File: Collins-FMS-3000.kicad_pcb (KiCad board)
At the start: 2 copper layers, 145 x 161 mm, 142 parts, among them J1 USB_B_Mini, J2 AVR-ISP-6, J3 Conn_02x04_Odd_Even, SW1 SW_Push_LED, SW10 SW_Push_LED, SW11 SW_Push_LED, SW12 SW_Push_LED, SW13 SW_Push_LED, SW14 SW_Push_LED, SW15 SW_Push_LED, SW16 SW_Push_LED, SW17 SW_Push_LED, SW18 SW_Push_LED, SW19 SW_Push_LED, SW2 SW_Push_LED, SW20 SW_Push_LED, SW21 SW_Push_LED, SW22 SW_Push_LED, SW23 SW_Push_LED, SW24 SW_Push_LED, SW25 SW_Push_LED, SW26 SW_Push_LED, SW27 SW_Push_LED, SW28 SW_Push_LED, SW29 SW_Push_LED, SW3 SW_Push_LED, SW30 SW_Push_LED, SW31 SW_Push_LED, SW32 SW_Push_LED, SW33 SW_Push_LED, SW34 SW_Push_LED, SW35 SW_Push_LED, SW36 SW_Push_LED, SW37 SW_Push_LED, SW38 SW_Push_LED, SW39 SW_Push_LED, SW4 SW_Push_LED, SW40 SW_Push_LED, SW41 SW_Push_LED, SW42 SW_Push_LED, SW43 SW_Push_LED, SW44 SW_Push_LED, SW45 SW_Push_LED, SW46 SW_Push_LED, SW47 SW_Push_LED, SW48 SW_Push_LED, SW49 SW_Push_LED, SW5 SW_Push_LED, SW50 SW_Push_LED, SW51 SW_Push_LED, SW52 SW_Push_LED, SW53 SW_Push_LED, SW54 SW_Push_LED, SW55 SW_Push_LED, SW56 SW_Push_LED, SW57 SW_Push_LED, SW58 SW_Push_LED, SW59 SW_Push_LED, SW6 SW_Push_LED, SW60 SW_Push_LED, SW61 SW_Push_LED, SW62 SW_Push_LED, SW63 SW_Push_LED, SW64 SW_Push_LED, SW65 SW_Push_LED, SW66 SW_Push_LED, SW67 SW_Push_LED, SW68 SW_Push_LED, SW69 SW_Push_LED, SW7 SW_Push_LED, SW8 SW_Push_LED, SW9 SW_Push_LED, U1 ATmega32U4-MU, U2 MCP23017_SO, U3 MCP23017_SO, U4 IS31FL3733B, Y1 16MHz

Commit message: More routing
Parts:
- R10, R11, R12, R13, R14, R15, R16, R17, R18, R19, R8, R9: moved to B.Cu
- moved R10 19.3 mm to (170.0, 61.2)
- moved R13 19.3 mm to (173.2, 61.2)
- moved R16 19.3 mm to (176.3, 61.2)
- moved R8 18.8 mm to (167.1, 60.7)
- moved R12 15.2 mm to (170.0, 59.2)
- moved R15 15.2 mm to (173.2, 59.2)
- moved R18 15.2 mm to (176.3, 59.2)
- moved R9 15.2 mm to (166.9, 59.2)
- moved R11 11.1 mm to (166.9, 57.1)
- moved R14 11.1 mm to (170.0, 57.1)
- moved R17 11.1 mm to (173.2, 57.1)
- moved R19 11.1 mm to (176.3, 57.1)
- moved R22 0.21 mm to (106.8, 28.7)
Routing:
- net /ButtonMatrix/ROW6: track 85.1 -> 290.1 mm, vias 0 -> 4
- net /ButtonMatrix/COL11: track 0.00 -> 196.9 mm
- net /LEDMatrix/SW7: track 13.9 -> 209.2 mm, vias 0 -> 4
- net /ButtonMatrix/ROW0: track 25.7 -> 211.7 mm, vias 0 -> 4
- net /LEDMatrix/SW1: track 0.00 -> 180.6 mm, vias 0 -> 4
- net /ButtonMatrix/COL0: track 0.30 -> 173.7 mm
- net /ButtonMatrix/ROW5: track 72.2 -> 245.3 mm, vias 0 -> 4
- net /ButtonMatrix/ROW1: track 32.1 -> 202.7 mm, vias 0 -> 4
- net /LEDMatrix/SW2: track 0.00 -> 165.5 mm, vias 0 -> 4
- net /ButtonMatrix/ROW4: track 55.7 -> 213.3 mm, vias 0 -> 4
- net /ButtonMatrix/ROW9: track 91.5 -> 246.9 mm, vias 2 -> 4
- net /ButtonMatrix/ROW2: track 40.1 -> 194.0 mm, vias 0 -> 2
- net /ButtonMatrix/ROW8: track 92.6 -> 244.2 mm
- net /ButtonMatrix/ROW7: track 83.8 -> 232.7 mm
- net /LEDMatrix/SW10: track 6.95 -> 154.7 mm, vias 0 -> 2
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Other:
- net class SW traces: trace_width 0.381 -> 0.25

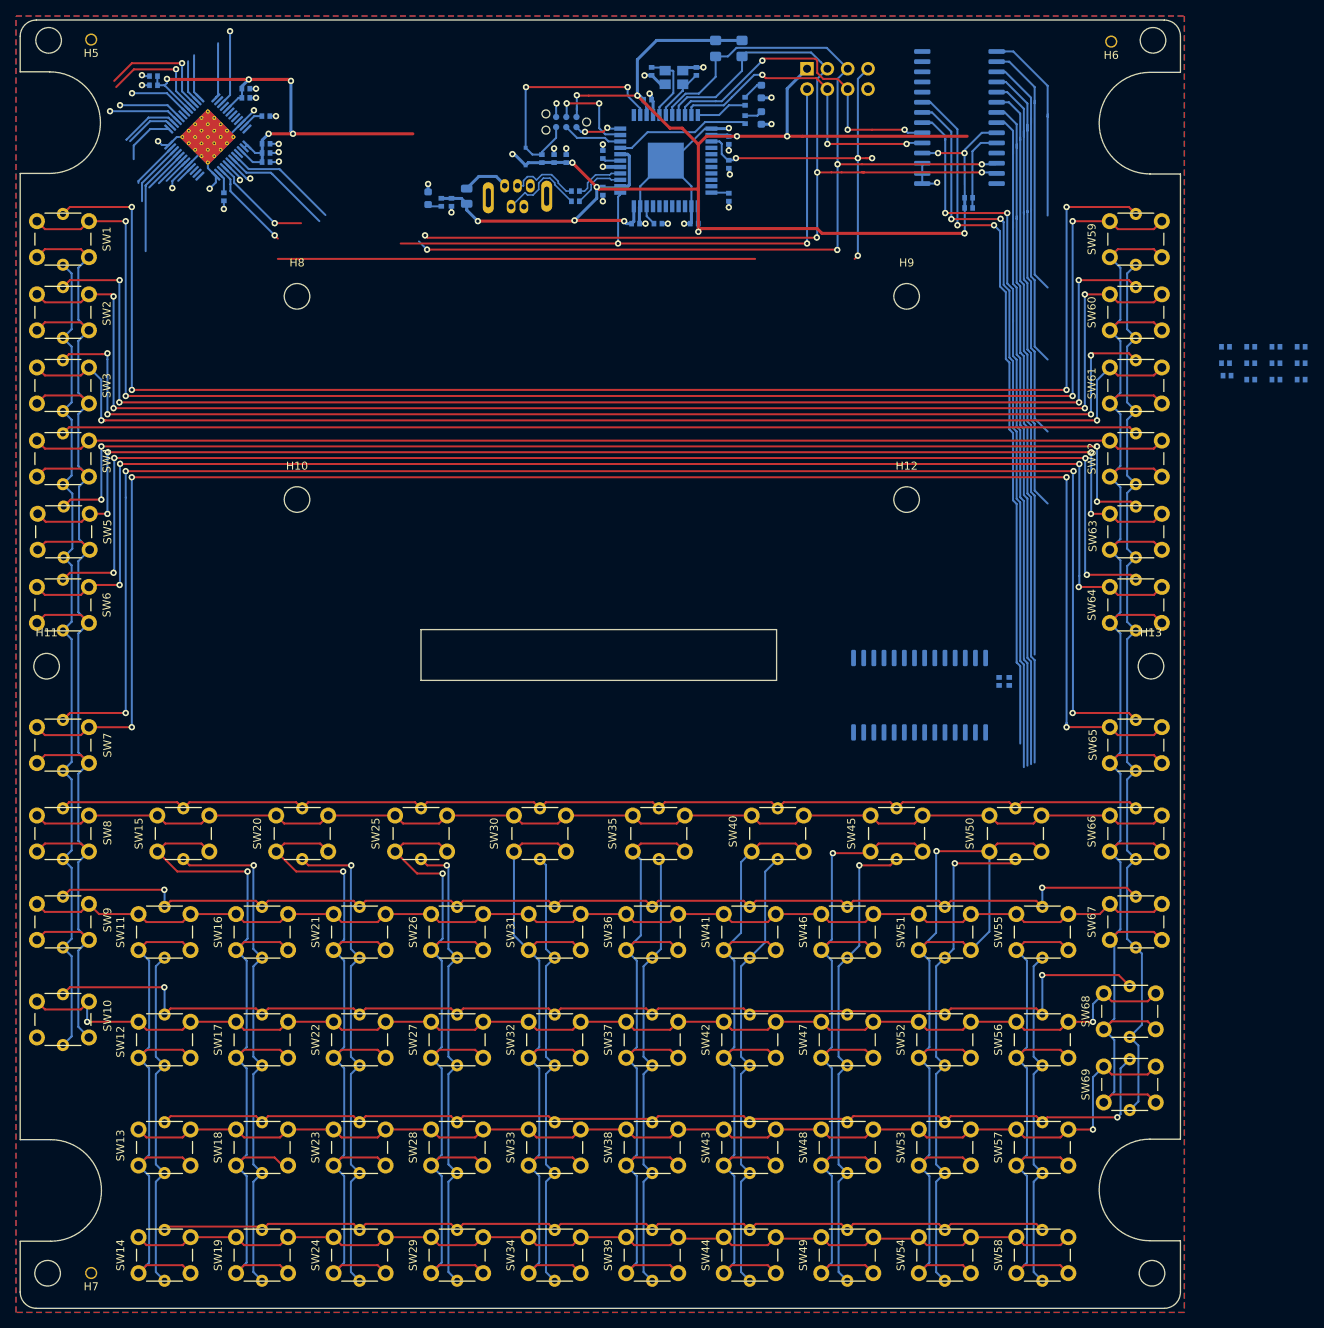
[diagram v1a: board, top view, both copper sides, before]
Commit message: More trace routing
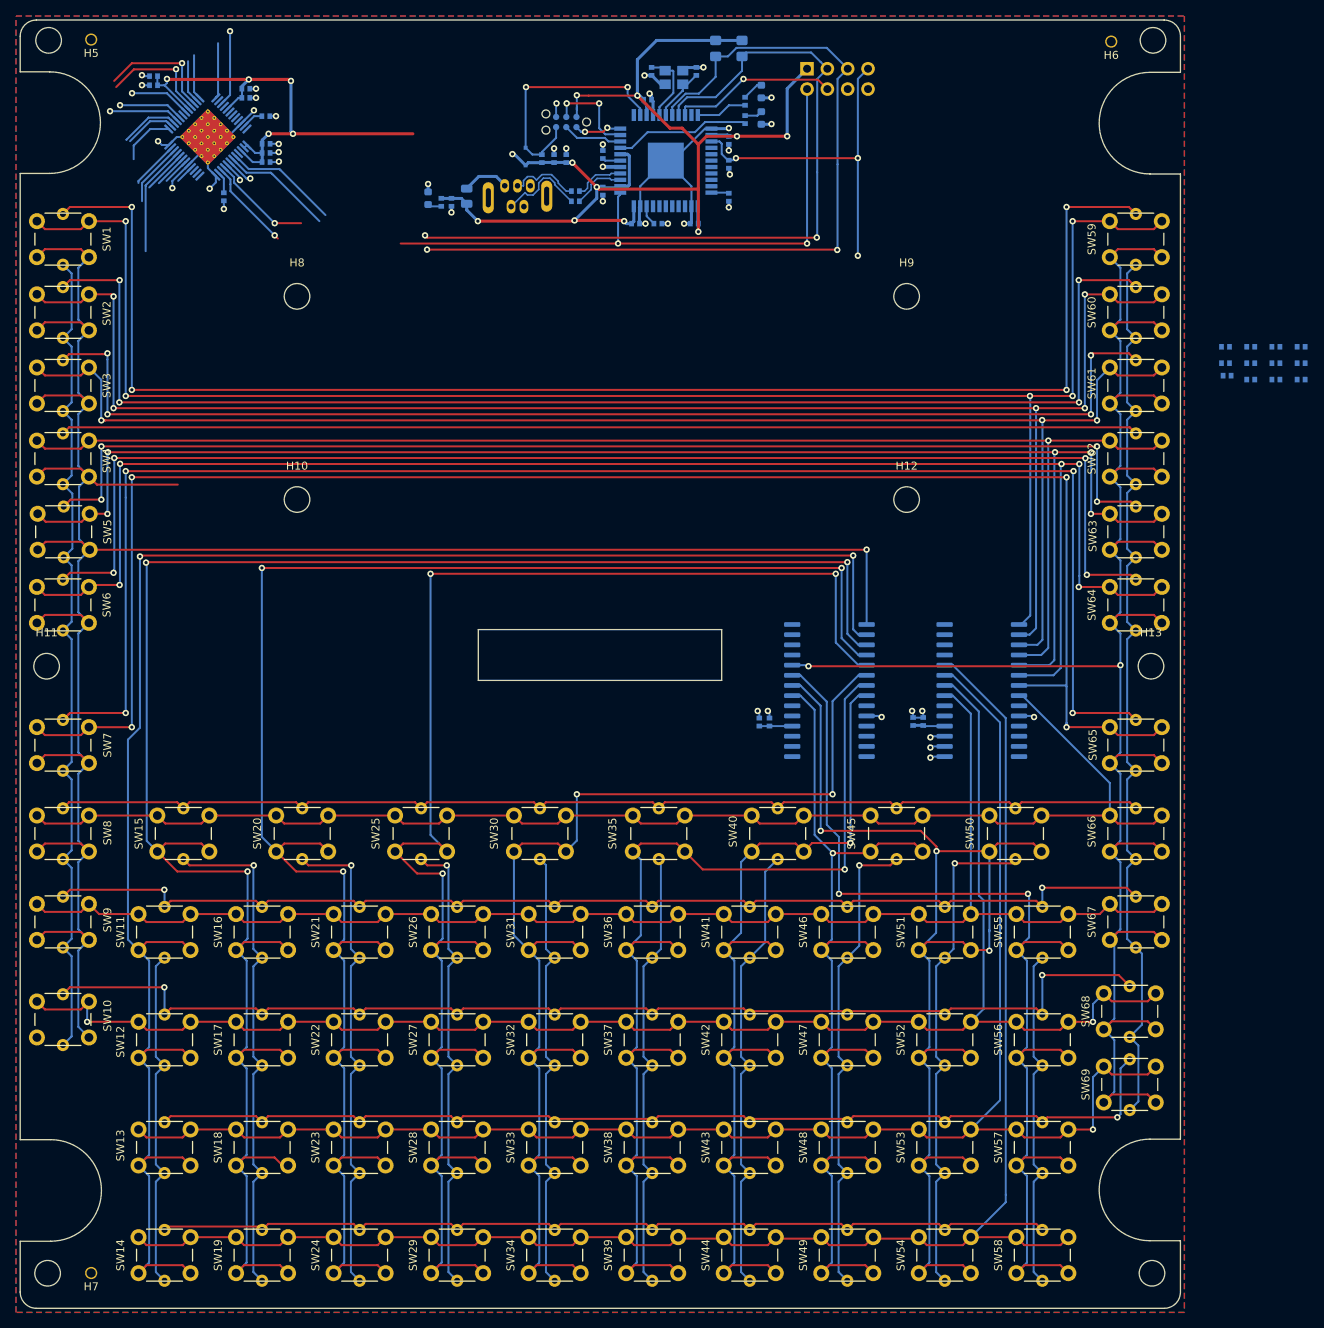
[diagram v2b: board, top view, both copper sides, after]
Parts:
- moved U2 71.7 mm to (136.4, 100.1)
- moved C1 65.8 mm to (127.8, 103.9), turned to 90 degrees
- moved C2 64.4 mm to (129.1, 103.9), turned to 90 degrees
- moved C3 30.4 mm to (109.9, 104.0)
- moved C4 30.4 mm to (108.6, 104.0)
- moved U3 11.3 mm to (117.3, 100.1), turned to 180 degrees
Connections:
- J3 pad 4: ROW_INTB -> ROW_INTA
- J3 pad 6: ROW_INTA -> Net-(J3-Pad6)
- U1 pad 21: ROW_INTB -> Net-(U1-Pad21)
- U2 pad 19: ROW_INTB -> Net-(U2-Pad19)
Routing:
- net /ButtonMatrix/COL1: track 73.0 -> 223.7 mm, vias 0 -> 2
- net /ButtonMatrix/COL2: track 103.3 -> 239.6 mm, vias 1 -> 3
- net /ButtonMatrix/COL3: track 100.2 -> 221.6 mm, vias 1 -> 3
- net /ButtonMatrix/COL0: track 173.7 -> 291.7 mm, vias 0 -> 1
- net /ButtonMatrix/COL4: track 97.6 -> 197.4 mm, vias 1 -> 3
- net /ButtonMatrix/ROW6: track 290.1 -> 210.8 mm
- net /ButtonMatrix/ROW11: track 125.0 -> 202.1 mm
- net +5V: track 290.8 -> 221.8 mm, vias 19 -> 16
- net /ButtonMatrix/ROW7: track 232.7 -> 168.8 mm
- net /ButtonMatrix/ROW8: track 244.2 -> 180.9 mm, vias 2 -> 0
- net SDB: track 117.6 -> 55.3 mm, vias 5 -> 4
- net /ButtonMatrix/COL10: track 73.0 -> 134.3 mm, vias 0 -> 2
- net /ButtonMatrix/COL5: track 93.4 -> 150.3 mm, vias 0 -> 2
- net /ButtonMatrix/ROW9: track 246.9 -> 200.8 mm, vias 4 -> 2
- net /ButtonMatrix/COL6: track 93.8 -> 139.5 mm, vias 0 -> 1
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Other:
- outline, holes or cut-outs redrawn
- board text removed: "RINTB"

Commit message: MCPs are routed!
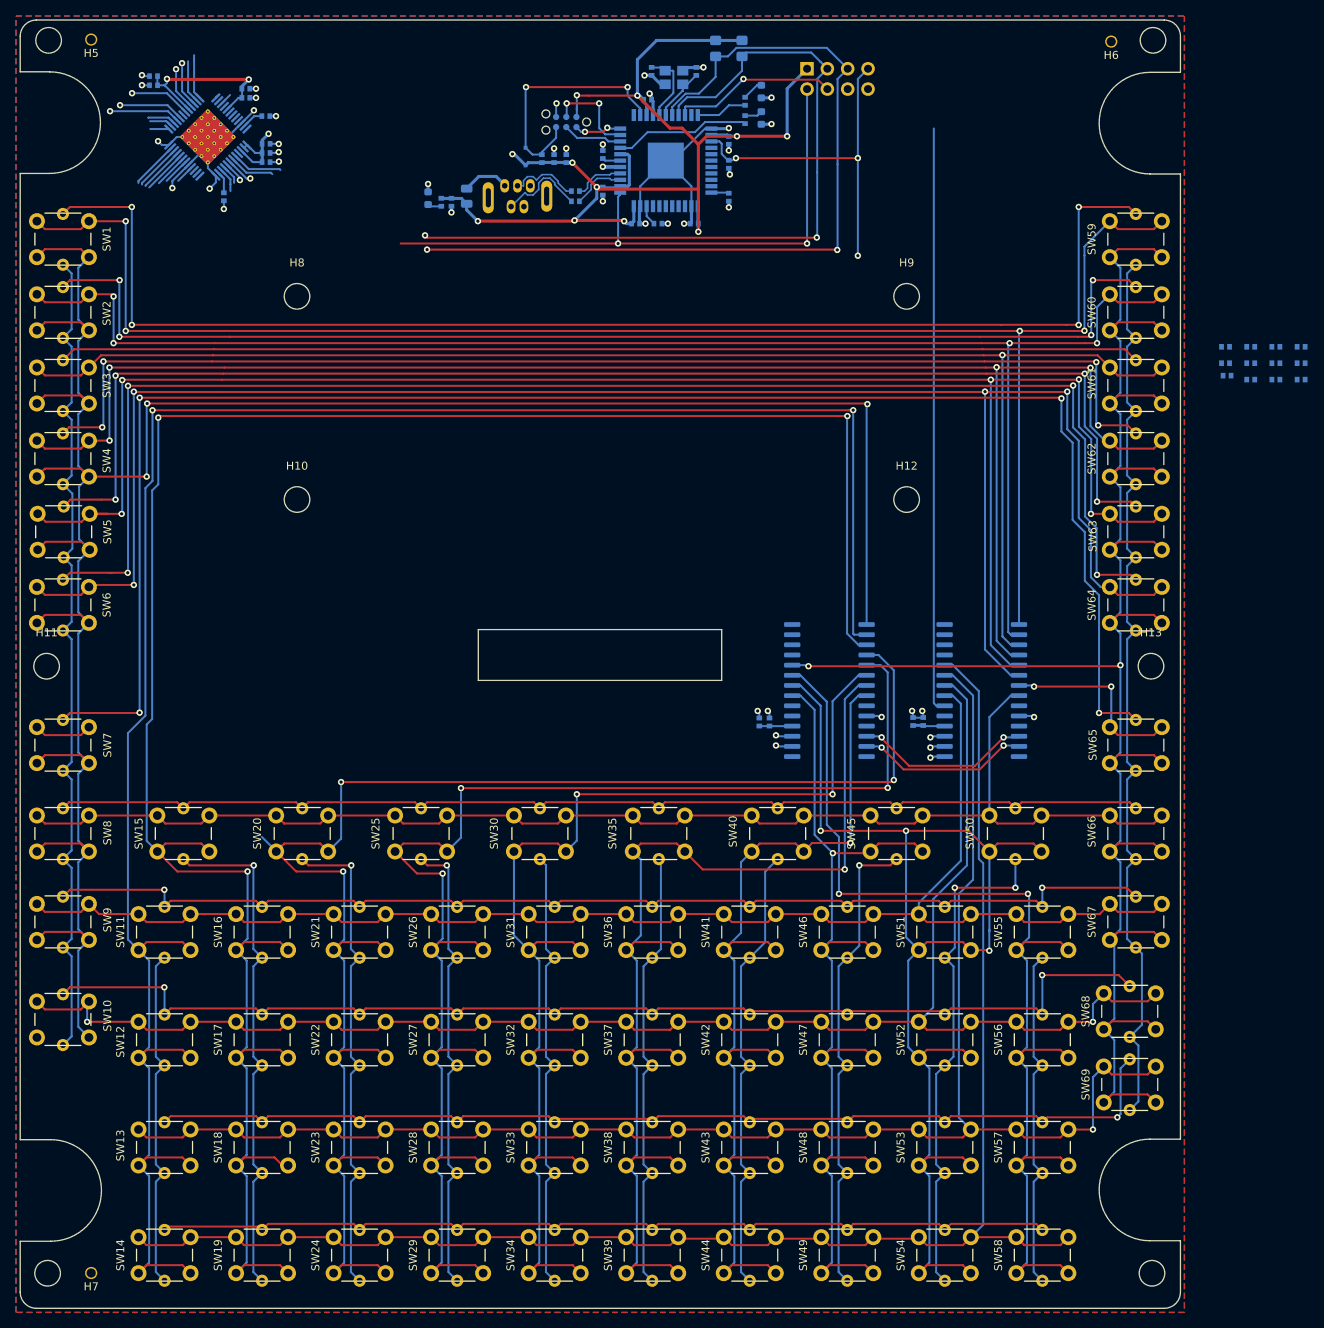
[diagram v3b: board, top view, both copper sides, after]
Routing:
- net /ButtonMatrix/ROW6: track 210.8 -> 31.4 mm, vias 4 -> 2
- net ROW_INTA: track 20.8 -> 94.1 mm
- net /ButtonMatrix/COL1: track 223.7 -> 259.6 mm
- net /ButtonMatrix/COL2: track 239.6 -> 275.1 mm
- net +5V: track 221.8 -> 191.7 mm, vias 16 -> 14
- net /ButtonMatrix/ROW4: track 188.3 -> 214.9 mm
- net /ButtonMatrix/ROW3: track 172.2 -> 197.2 mm, vias 1 -> 4
- net /ButtonMatrix/COL3: track 221.6 -> 199.2 mm
- net /ButtonMatrix/ROW5: track 204.3 -> 226.4 mm, vias 5 -> 4
- net /ButtonMatrix/COL4: track 197.4 -> 177.0 mm
- net /LEDMatrix/SW5: track 152.4 -> 169.6 mm
- net /LEDMatrix/SW6: track 168.8 -> 185.5 mm
- net /LEDMatrix/SW2: track 165.5 -> 148.8 mm
- net /LEDMatrix/SW1: track 180.6 -> 164.3 mm
- net /LEDMatrix/SW4: track 138.1 -> 154.2 mm, vias 0 -> 4
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
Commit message: Fully routed and passes DRC!
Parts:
- moved R19 117.0 mm to (148.3, 170.7), turned to 180 degrees
- moved R18 92.0 mm to (157.1, 149.1)
- moved R17 84.4 mm to (157.1, 140.0)
- moved R16 70.1 mm to (157.7, 128.8)
- moved C22 66.9 mm to (47.6, 89.7)
- moved C23 66.9 mm to (59.1, 91.3)
- moved C25 66.9 mm to (47.6, 88.6)
- moved R6 66.9 mm to (61.6, 93.6)
- moved U4 66.9 mm to (54.4, 96.2)
- moved C24 66.9 mm to (61.7, 97.0)
- moved C26 66.9 mm to (59.1, 90.1)
- moved C27 66.9 mm to (61.7, 98.2)
- moved C28 66.9 mm to (61.7, 99.3)
- moved R7 66.9 mm to (56.4, 103.6)
- moved R15 60.7 mm to (157.7, 117.9)
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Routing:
- net +5V: track 191.7 -> 546.4 mm, vias 14 -> 25
- net /ButtonMatrix/ROW6: track 31.4 -> 229.1 mm, vias 2 -> 5
- net /LEDMatrix/CS11: track 44.6 -> 183.2 mm, vias 0 -> 2
- net SDB: track 47.0 -> 169.9 mm, vias 3 -> 6
- net /LEDMatrix/CS10: track 63.5 -> 182.7 mm, vias 2 -> 5
- net /LEDMatrix/CS12: track 114.7 -> 222.8 mm, vias 0 -> 3
- net /LEDMatrix/CS9: track 60.7 -> 168.3 mm, vias 1 -> 4
- net I2C_SDA: track 123.0 -> 222.1 mm, vias 4 -> 5
- net /LEDMatrix/CS8: track 62.5 -> 154.7 mm, vias 0 -> 2
- net I2C_SCL: track 131.0 -> 223.1 mm, vias 4 -> 5
- net /LEDMatrix/SW12: track 118.9 -> 205.9 mm, vias 0 -> 2
- net /LEDMatrix/CS7: track 61.4 -> 144.0 mm, vias 0 -> 4
- net /LEDMatrix/SW2: track 148.8 -> 230.3 mm, vias 4 -> 7
- net /LEDMatrix/SW1: track 164.3 -> 245.3 mm, vias 4 -> 7
- net /LEDMatrix/SW3: track 137.6 -> 217.4 mm, vias 0 -> 3
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
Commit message: Fix some bugs, add silkscreen
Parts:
- moved C4 17.9 mm to (126.5, 102.5), turned to 270 degrees
- moved C1 17.6 mm to (145.3, 102.6), turned to 270 degrees
- moved C3 15.4 mm to (125.2, 102.5), turned to 270 degrees
- moved C2 15.1 mm to (144.1, 102.6), turned to 270 degrees
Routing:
- net +5V: track 546.4 -> 561.9 mm, vias 25 -> 24
- net /ButtonMatrix/COL3: track 196.6 -> 204.2 mm, vias 3 -> 5
- net /ButtonMatrix/COL4: track 177.0 -> 184.0 mm, vias 3 -> 5
- net GND: track 116.4 -> 121.1 mm, vias 46 -> 44
- net /LEDMatrix/CS11: track 183.2 -> 186.1 mm
- net /ButtonMatrix/ROW6: track 229.1 -> 231.4 mm
- net /ButtonMatrix/ROW7: track 171.5 -> 173.4 mm, vias 0 -> 2
- net /ButtonMatrix/COL11: track 238.1 -> 238.7 mm
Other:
- board text added: "%%version%%"
- board text added: "COL0"
- board text added: "CS1"
- board text added: "Collins FMS 3000 Neil Enns neile@live.com %%date%% %%version%%"
- board text added: "ROW0"
- board text added: "SW1"
